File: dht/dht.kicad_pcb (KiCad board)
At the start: 2 copper layers, 73.3 x 38 mm, 7 parts, among them J1 Conn_02x04_Top_Bottom, J2 Conn_01x02, J3 Conn_01x03_MountingPin

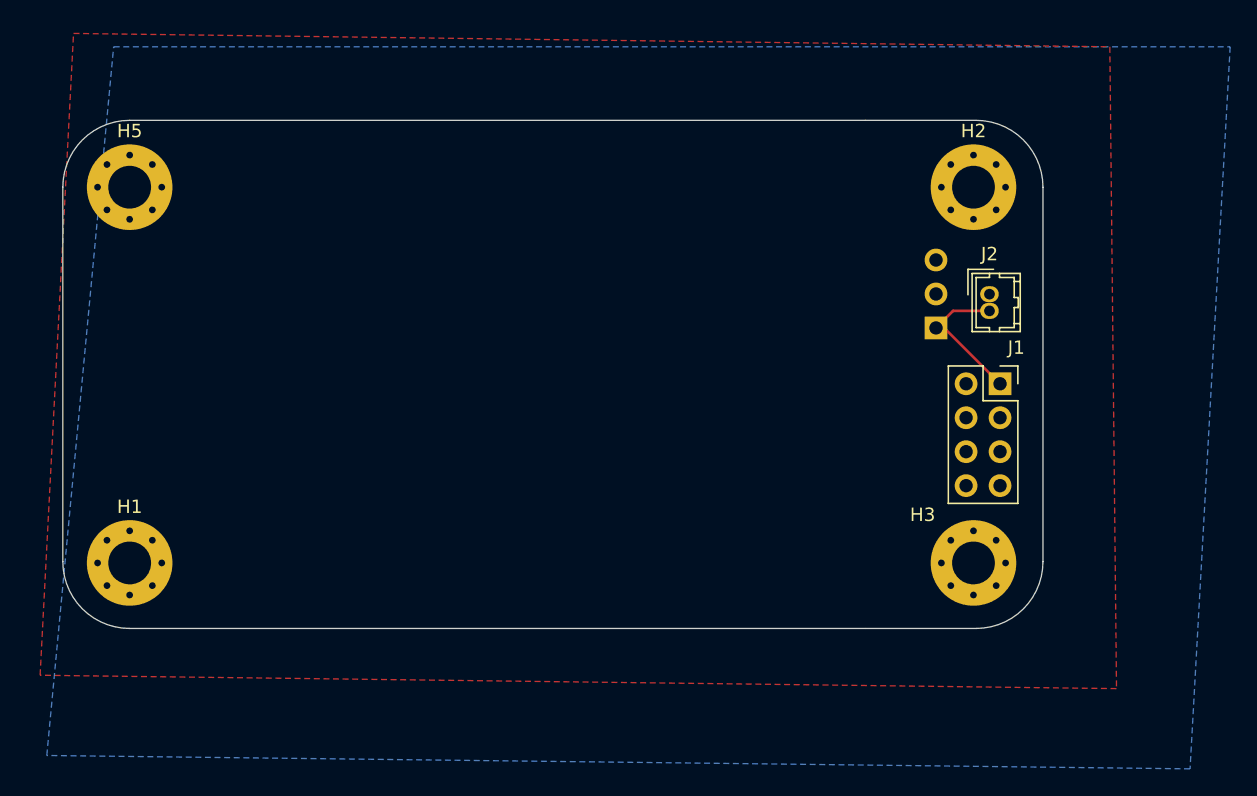
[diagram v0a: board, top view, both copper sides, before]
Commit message: orderd PCB V1 added step file for CAD
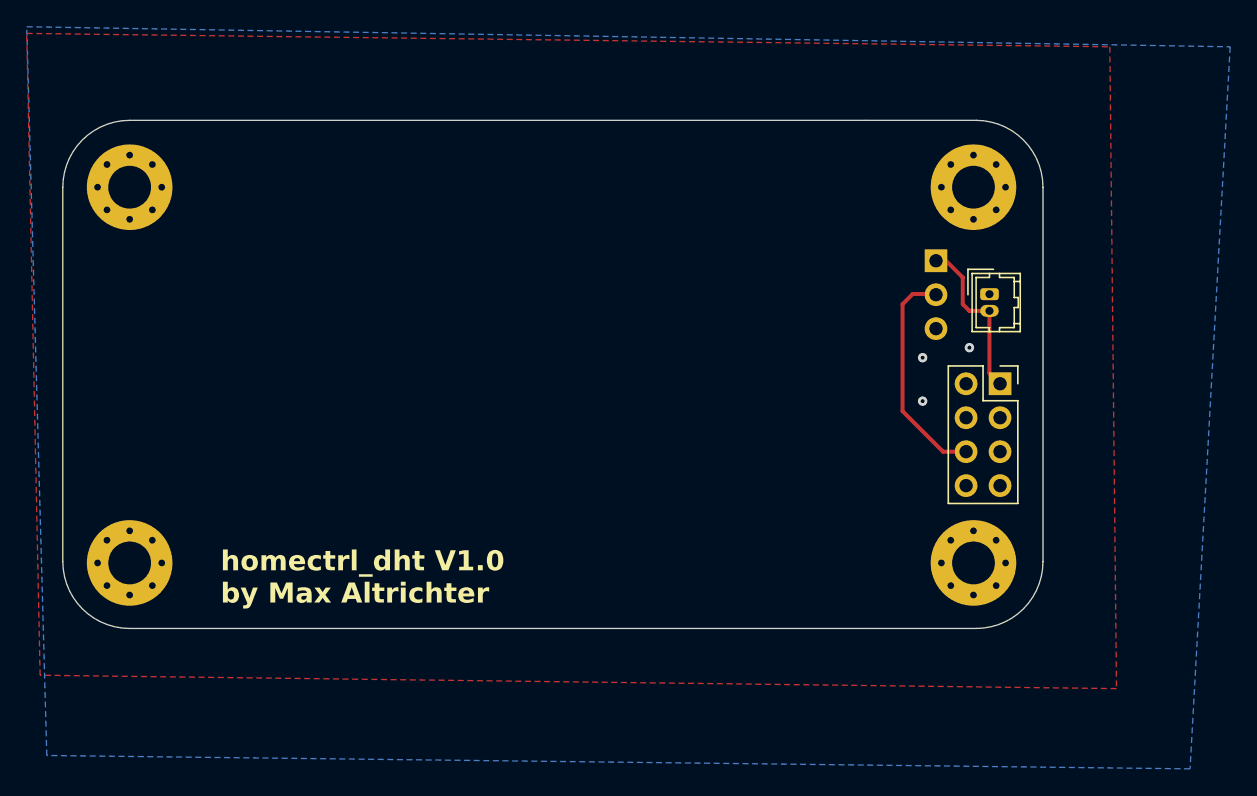
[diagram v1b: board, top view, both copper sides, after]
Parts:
- moved J3 5.03 mm to (162.0, 80.5), turned to 180 degrees
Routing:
- net IO2: track 0.00 -> 16.8 mm
- net VCC: track 11.0 -> 12.5 mm
- net GND: vias 0 -> 3
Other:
- board text added: "homectrl_dht V1.0 by Max Altrichter"
